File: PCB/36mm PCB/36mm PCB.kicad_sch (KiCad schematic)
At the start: 64 parts, among them IC1 PCF2003DUS, IC2 BMM350, IC3 STM32L011E4Y6TR, IC4 TPS22991BRAAR, IC5 MCP73831-2ACI_MC, IC6 AS5510-DWLM, Q3 2N7002KQBZ, Q4 2N7002KQBZ, Q5 2N7002KQBZ, Q6 2N7002KQBZ, Q7 2N7002KQBZ, SW5 SW_MEC_5E, U1 BMP581, Y1 ABS04W-32.768KHZ-4-D2-T5

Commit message: PCB 2.0
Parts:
- removed C1, C10, C11, C13, C16, C4, C5, C9: 100n, Capacitor_SMD:C_0201_0603Metric, symbol Device:C
- removed C12: 220n, Capacitor_SMD:C_0201_0603Metric, symbol Device:C
- removed C14, C15: 4.7u, Capacitor_SMD:C_0201_0603Metric, symbol Device:C
- removed C2, C3, C6, C7, CLPT1, CSPT1: 1u, Capacitor_SMD:C_0201_0603Metric, symbol Device:C
- removed C8: 200n, Capacitor_SMD:C_0201_0603Metric, symbol Device:C
- removed D1, D2: D, Diode_SMD:D_0201_0603Metric, symbol Device:D
- removed IC1: PCF2003DUS, SamacSys_Parts:PCF2003DUS, symbol SamacSys_Parts:PCF2003DUS
- removed IC2: BMM350, SamacSys_Parts:BGA9C40P3X3_128X128X54, symbol SamacSys_Parts:BMM350
- removed IC3: STM32L011E4Y6TR, SamacSys_Parts:BGA25C40P5X5_213X207X58, symbol SamacSys_Parts:STM32L011E4Y6TR
- removed IC4: TPS22991BRAAR, SamacSys_Parts:TPS22991BRAAR, symbol SamacSys_Parts:TPS22991BRAAR
- removed IC5: MCP73831-2ACI_MC, SamacSys_Parts:SON50P300X200X100-9N-D, symbol SamacSys_Parts:MCP73831-2ACI_MC
- removed IC6: AS5510-DWLM, BGA6C40P3X2_138X102X63, symbol SamacSys_Parts:AS5510-DWLM
- removed L1: 27n, Inductor_SMD:L_0201_0603Metric, symbol Device:L
- removed L2, L3: L, SamacSys_Parts:Miyota 2035, symbol Device:L
- removed Q3, Q4, Q5, Q6, Q7: 2N7002KQBZ, SamacSys_Parts:2N7002KQBZ, symbol SamacSys_Parts:2N7002KQBZ
- removed R1, R2, R3, R9: 0, Resistor_SMD:R_0201_0603Metric, symbol Device:R
- removed R10, R13, R14, R15, R16, R19: 100k, Resistor_SMD:R_0201_0603Metric, symbol Device:R
- removed R17: 1k, Resistor_SMD:R_0201_0603Metric, symbol Device:R
- removed R18: 47k, Resistor_SMD:R_0201_0603Metric, symbol Device:R
- removed R4, R5, R6, R7, R8: 2k, Resistor_SMD:R_0201_0603Metric, symbol Device:R
- removed SW5: SW_MEC_5E, SamacSys_Parts:Wurth side button 434331013822, symbol Switch:SW_MEC_5E
- removed TP1: GND_PCF2003, TestPoint:TestPoint_Pad_D1.0mm, symbol Connector:TestPoint
- removed TP14: B+, TestPoint:TestPoint_Pad_D1.0mm, symbol Connector:TestPoint
- removed TP15: B-, TestPoint:TestPoint_Pad_D1.0mm, symbol Connector:TestPoint
- removed TP2: VDD_PCF2003, TestPoint:TestPoint_Pad_D1.0mm, symbol Connector:TestPoint
- removed TP5: SWDIO, TestPoint:TestPoint_Pad_D1.0mm, symbol Connector:TestPoint
- removed TP6: SWCLK, TestPoint:TestPoint_Pad_D1.0mm, symbol Connector:TestPoint
- removed TP7: NRST, TestPoint:TestPoint_Pad_D1.0mm, symbol Connector:TestPoint
- removed TPS3424-1: ~, Package_TO_SOT_SMD:SOT-583-8, symbol SamacSys_Parts:TPS3424-8
- removed U1: BMP581, SamacSys_Parts:BMP581, symbol SamacSys_Parts:BMP581
- removed Y1: ABS04W-32.768KHZ-4-D2-T5, SamacSys_Parts:ABS04W32768KHZ4D2T5, symbol SamacSys_Parts:ABS04W-32.768KHZ-4-D2-T5
- added C23, C30: 1u, Capacitor_SMD:C_0402_1005Metric, symbol Device:C
- added C24, C27, C28, C29: 100n, Capacitor_SMD:C_0201_0603Metric, symbol Device:C_Small
- added R19, R20: 100k, Resistor_SMD:R_0201_0603Metric, symbol Device:R_Small
- added TP19: NRST, SamacSys_Parts:Pogo pin 1x1, symbol Connector:TestPoint
- added TP20: 3.3V, SamacSys_Parts:Pogo pin 1x1, symbol Connector:TestPoint
- added TP21: VSS, SamacSys_Parts:Pogo pin 1x1, symbol Connector:TestPoint
- added U2: STM32L011F4Ux, Package_DFN_QFN:ST_UFQFPN-20_3x3mm_P0.5mm, symbol MCU_ST_STM32L0:STM32L011F4Ux
- TP17: value Charge+ -> SWDIO; footprint TestPoint:TestPoint_Pad_D1.0mm -> SamacSys_Parts:Pogo pin 1x1
- TP18: value Charge- -> SWCLK; footprint TestPoint:TestPoint_Pad_D1.0mm -> SamacSys_Parts:Pogo pin 1x1
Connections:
- net GND: now also C23.2, C24.1, C27.1, C28.1, C29.1, C30.2, R20.1, TP21.1, U2.12 (VSS); no longer TP18.1
- net NRST: now also C27.2, TP19.1, U2.3 (NRST)
- net Charge+ renamed SWDIO
- net SWDIO: now also U2.16 (PA13)
- new net: C28.2, R19.2, R20.2, U2.5 (PA0)
- new net +3.3V: C23.1, C24.2, C29.2, C30.1, TP20.1, U2.13 (VDD), U2.4 (VDDA)
- new net ADC_Vbat: R19.1
- new net BMP581_INT: U2.15 (PA10)
- new net Button press: U2.20 (PB9)
- new net H_Tim1: U2.11 (PB1)
- new net H_Tim2: U2.8 (PA5)
- new net I2C_SCL: U2.18 (PB6)
- new net I2C_SDA: U2.19 (PB7)
- new net KeepOn: U2.10 (PA7)
- new net Kill: U2.2 (PC15)
- new net L-S press INT: U2.1 (PC14)
- new net SWCLK: TP18.1, U2.17 (PA14)
- no-connect marks 14 -> 4
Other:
- added sheet Main dial (MainDial.kicad_sch)
- added sheet Peripherals (peripherals.kicad_sch)
- added sheet Power (Power.kicad_sch)
- added sheet Subdial (Subdial.kicad_sch)
- note added: "STM32"
- note removed: "5pF Crystal"
- note removed: "Barometer"
- note removed: "Batteries"
- note removed: "Charger"
- note removed: "Compass"
- note removed: "I2C peripherals"
- note removed: "Power ON/OFF"
- note removed: "STM32L011E4Y6TR"
- note removed: "Subdial driving H bridge"
- note removed: "Watch IC controller"

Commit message: Modifs Mathieu
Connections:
- net H_Tim1: now also U2.6 (PA1); no longer U2.11 (PB1)
- net KeepOn: now also U2.9 (PA6); no longer U2.10 (PA7)
- new net PCF_Reset: U2.10 (PA7)
- no-connect marks 4 -> 3
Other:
- sheet Main dial ports: added PCF_Reset; removed none
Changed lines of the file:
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@@
 	)
 	(no_connect
-		(at 198.12 82.55)
-	)
-	(no_connect
-		(at 198.12 90.17)
+		(at 172.72 92.71)
 	)
 	(no_connect
@@
 	)
 	(label "KeepOn"
-		(at 198.12 92.71 0)
+		(at 198.12 90.17 0)
 		(effects
 			(font
@@
 	)
 	(label "H_Tim1"
-		(at 172.72 92.71 180)
-		(effects
-			(font
-				(size 1.27 1.27)
-			)
-			(justify right bottom)
+		(at 198.12 82.55 0)
+		(effects
+			(font
+				(size 1.27 1.27)
+			)
+			(justify left bottom)
+		)
+	)
+	(label "PCF_Reset"
+		(at 85.725 43.18 0)
+		(effects
+			(font
+				(size 1.27 1.27)
+			)
+			(justify left bottom)
 		)
 	)
@@
 	(label "ADC_Vbat"
 		(at 107.95 147.32 90)
+		(effects
+			(font
+				(size 1.27 1.27)
+			)
+			(justify left bottom)
+		)
+	)
+	(label "PCF_Reset"
+		(at 198.12 92.71 0)
 		(effects
 			(font
@@
 			)
 		)
+		(pin "PCF_Reset" input
+			(at 85.725 43.18 0)
+			(effects
+				(font
+					(size 1.27 1.27)
+				)
+				(justify right)
+			)
+		)

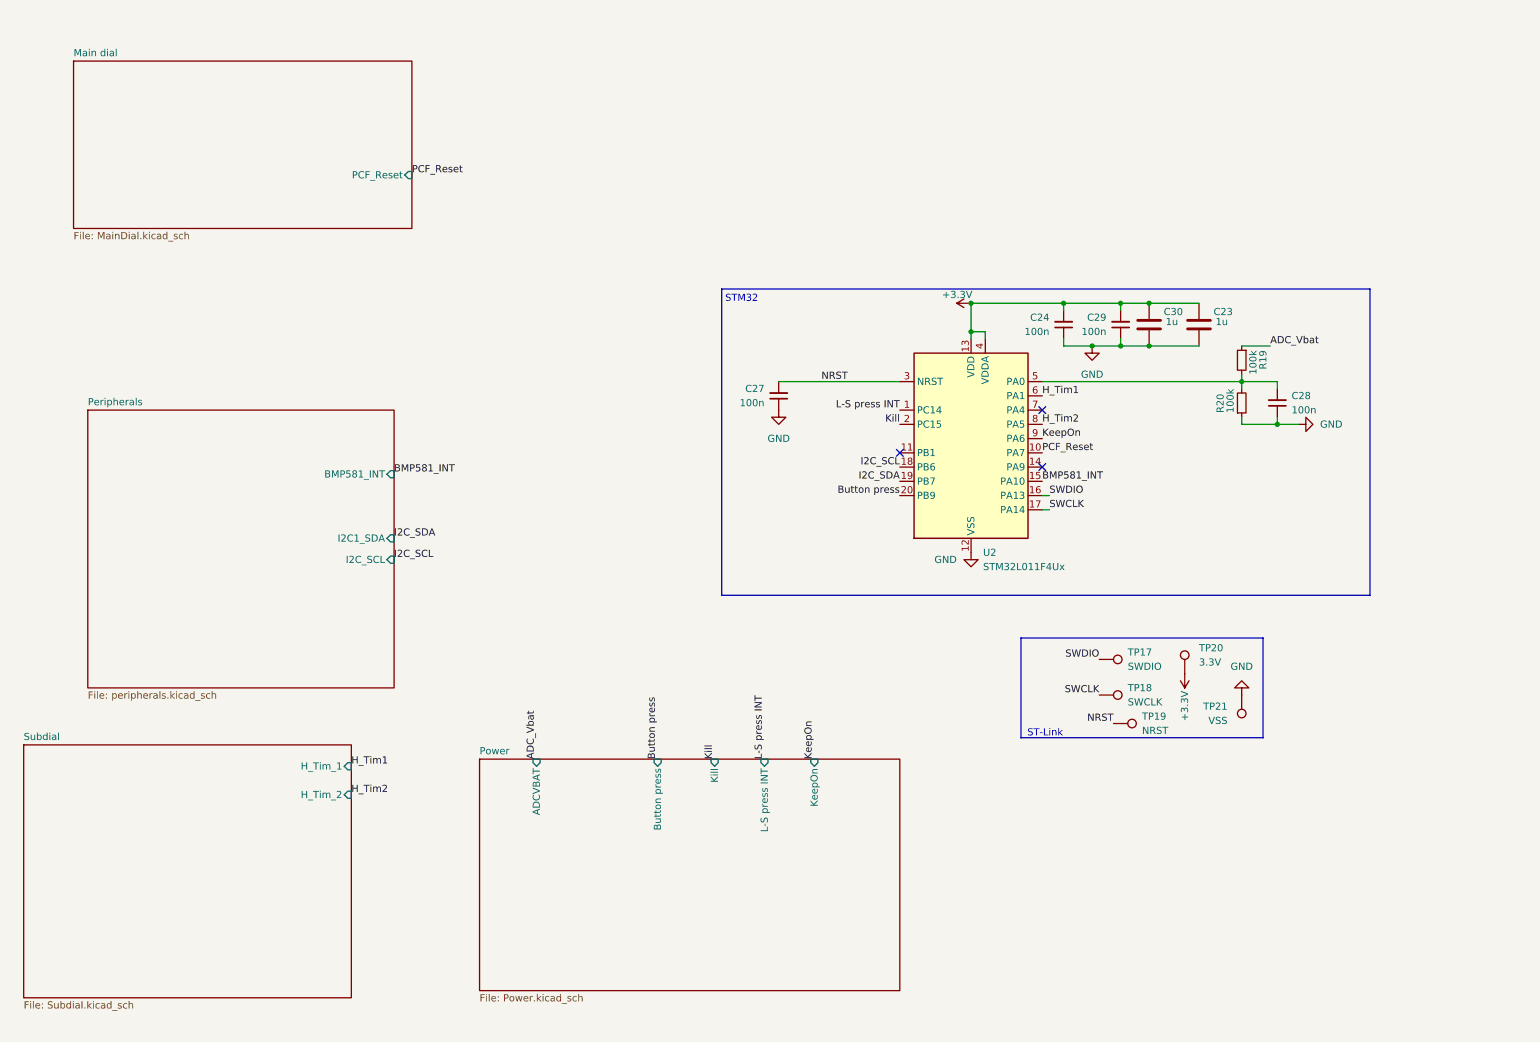
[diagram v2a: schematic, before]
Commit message: STM32 BLE + H chip
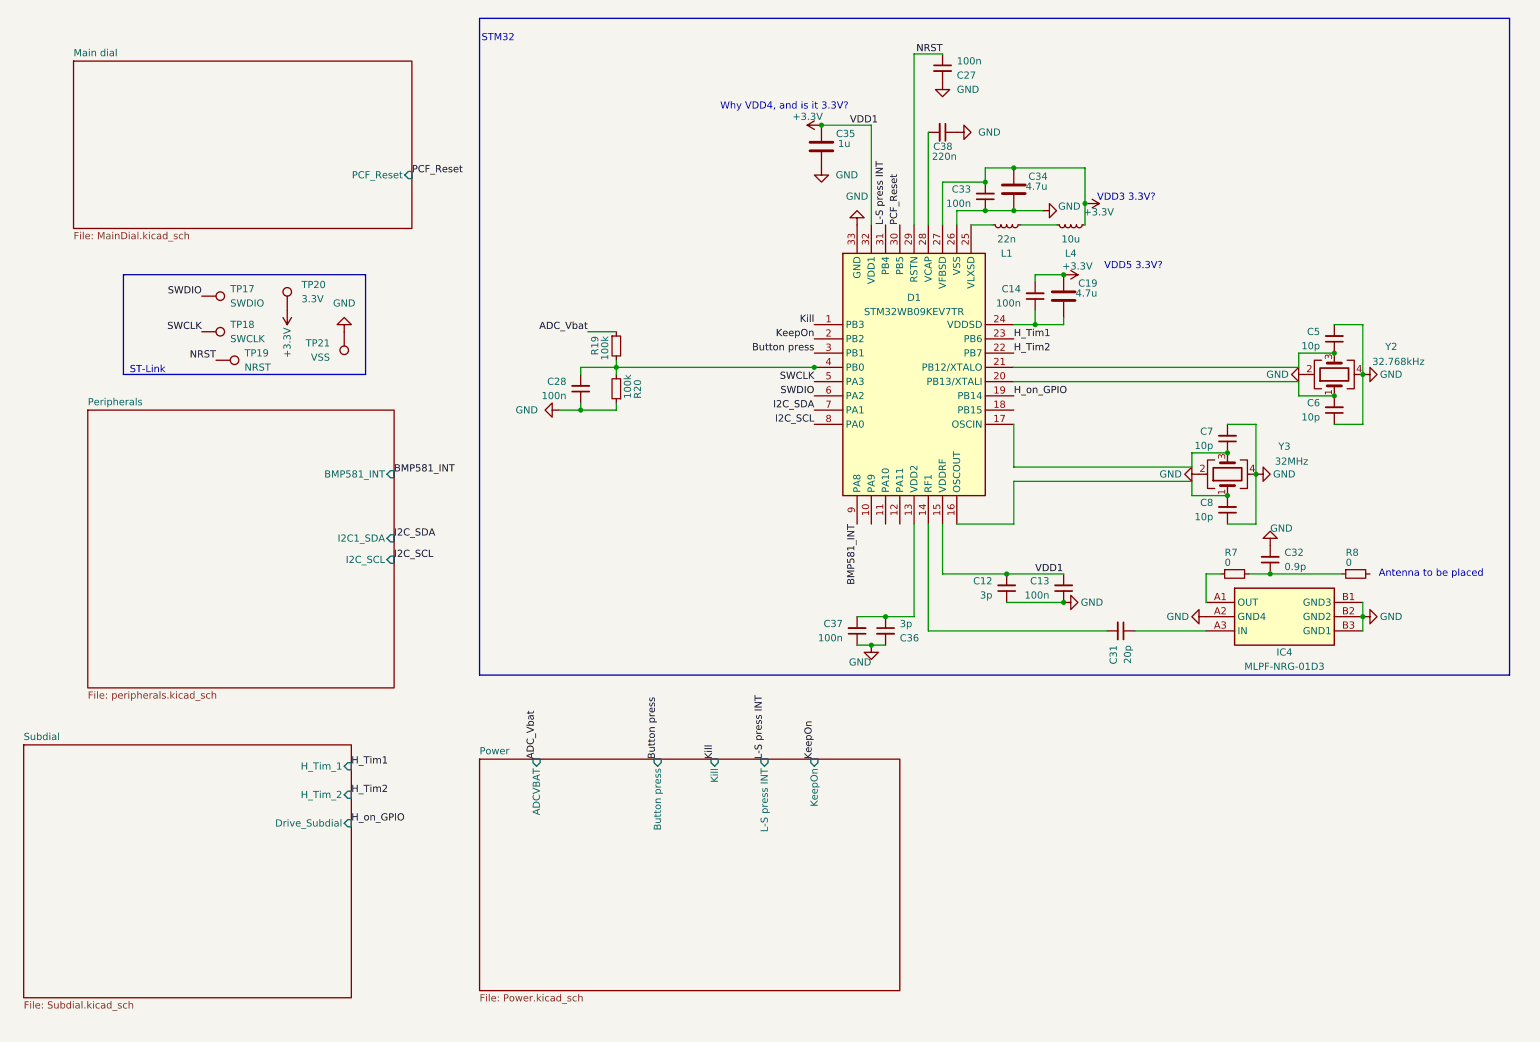
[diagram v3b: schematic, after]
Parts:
- removed C23, C30: 1u, Capacitor_SMD:C_0402_1005Metric, symbol Device:C
- removed C24, C29: 100n, Capacitor_SMD:C_0201_0603Metric, symbol Device:C_Small
- removed U2: STM32L011F4Ux, Package_DFN_QFN:ST_UFQFPN-20_3x3mm_P0.5mm, symbol MCU_ST_STM32L0:STM32L011F4Ux
- added C12, C36: 3p, Capacitor_SMD:C_0201_0603Metric, symbol Device:C_Small
- added C13, C14, C33, C37: 100n, Capacitor_SMD:C_0201_0603Metric, symbol Device:C_Small
- added C19, C34: 4.7u, Capacitor_SMD:C_0402_1005Metric, symbol Device:C
- added C31: 20p, Capacitor_SMD:C_0201_0603Metric, symbol Device:C_Small
- added C32: 0.9p, Capacitor_SMD:C_0201_0603Metric, symbol Device:C_Small
- added C35: 1u, Capacitor_SMD:C_0402_1005Metric, symbol Device:C
- added C38: 220n, Capacitor_SMD:C_0201_0603Metric, symbol Device:C_Small
- added C5, C6, C7, C8: 10p, Capacitor_SMD:C_0201_0603Metric, symbol Device:C_Small
- added D1: STM32WB09KEV7TR, QFN50P500X500X100-33N-D, symbol SamacSys_Parts:STM32WB09KEV7TR
- added IC4: MLPF-NRG-01D3, CSPG_2025, symbol SamacSys_Parts:MLPF-NRG-01D3
- added L1: 22n, symbol Device:L_Small
- added L4: 10u, symbol Device:L_Small
- added R7, R8: 0, Resistor_SMD:R_0201_0603Metric, symbol Device:R_Small
- added Y2: 32.768kHz, symbol Device:Crystal_GND24
- added Y3: 32MHz, symbol Device:Crystal_GND24
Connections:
- net +3.3V: now also C12.2, C13.2, C14.2, C19.1, C33.2, C34.1, C35.1, D1.15 (VDDRF), D1.27 (VFBSD), D1.32 (VDD1), L4.2
- net BMP581_INT: now also D1.9 (PA8)
- net Button press: now also D1.3 (PB1)
- net GND: now also C27.2, C12.1, C13.1, C32.2, C33.1, C34.2, C35.2, C36.2, C37.1, C38.1, C5.2, C6.1, C7.2, C8.1, D1.26 (VSS), D1.33 (GND), IC4.A2 (GND4), IC4.B1 (GND3), IC4.B2 (GND2), IC4.B3 (GND1), Y2.2, Y2.4, Y3.2, Y3.4; no longer C27.1
- net H_Tim1: now also D1.23 (PB6)
- net H_Tim2: now also D1.22 (PB7)
- net I2C_SCL: now also D1.8 (PA0)
- net I2C_SDA: now also D1.7 (PA1)
- net KeepOn: now also D1.2 (PB2)
- net Kill: now also D1.1 (PB3)
- net L-S press INT: now also D1.31 (PB4)
- net NRST: now also C27.1, D1.29 (RSTN); no longer C27.2
- net PCF_Reset: now also D1.30 (PB5)
- net SWCLK: now also D1.5 (PA3)
- net SWDIO: now also D1.6 (PA2)
- net at C28.2, R19.2, R20.2: now also D1.4 (PB0)
- new net: C36.1, C37.2, D1.13 (VDD2)
- new net: C31.2, D1.14 (RF1)
- new net: C8.2, D1.16 (OSCOUT), Y3.1
- new net: C7.1, D1.17 (OSCIN), Y3.3
- new net: C6.2, D1.20 (PB13/XTALI), Y2.1
- new net: C5.1, D1.21 (PB12/XTALO), Y2.3
- new net: C14.1, C19.2, D1.24 (VDDSD)
- new net: D1.25 (VLXSD), L1.1
- new net: C38.2, D1.28 (VCAP)
- new net: C32.1, R7.2, R8.1
- new net: IC4.A1 (OUT), R7.1
- new net: C31.1, IC4.A3 (IN)
- new net: L1.2, L4.1
- new net H_on_GPIO: D1.19 (PB14)
- no-connect marks 3 -> 0
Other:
- sheet Subdial ports: added Drive_Subdial; removed none
- note added: "Antenna to be placed"
- note added: "VDD3 3.3V?"
- note added: "VDD5 3.3V?"
- note added: "Why VDD4, and is it 3.3V?"
- moved on the sheet: C27, C28, R19, R20, TP17, TP18, TP19, TP20, TP21
